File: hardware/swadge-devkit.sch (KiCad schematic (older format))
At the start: 59 parts, among them J1 USB_B_Micro, SW1 SW_SPDT, SW2 4-1437565-2, SW3 4-1437565-2, SW4 4-1437565-2, SW5 4-1437565-2, U1 ESP-12F, U2 MCP6001-OT, U3 MSA300, U4 AP1117-33, U5 BUS_PCIexpress, U6 DISP_OLED_UG-2864HSWEG01, U7 SAO, U9 MMA8452Q

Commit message: #14 Replaced ESP-12F with ESP-WROOM-02D
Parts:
- removed U1: ESP-12F, Swadge_Parts:ESP-12E_SMD, symbol Swadge_Parts:ESP-12F
- added U?: ESP-13-WROOM-02D, Swadge_Parts:ESP-13-WROOM-02, symbol Swadge_Parts:ESP-13-WROOM-02D
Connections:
- wire segments 242 -> 245
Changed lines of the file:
@@
 	1    0    0    -1
 $EndComp
-Text GLabel 1150 3150 0    50   Input ~ 0
-ADC_PIN
-Text GLabel 1150 3450 0    50   Input ~ 0
-AUD_PWR
 $Comp
 L Swadge_Parts:R_US R1
@@
 F 3 "" H 2800 1500 50  0001 C CNN
 	1    2800 1500
-	1    0    0    -1
-$EndComp
-$Comp
-L power:GND #PWR0102
-U 1 1 5C3A2494
-P 3050 3750
-F 0 "#PWR0102" H 3050 3500 50  0001 C CNN
-F 1 "GND" H 3055 3577 50  0000 C CNN
-F 2 "" H 3050 3750 50  0001 C CNN
-F 3 "" H 3050 3750 50  0001 C CNN
-	1    3050 3750
 	1    0    0    -1
 $EndComp
@@
 	1    0    0    -1
 $EndComp
-Text GLabel 3050 3150 2    50   Input ~ 0
-RX
-Text GLabel 3050 3050 2    50   Input ~ 0
-TX
 Text GLabel 3900 1300 1    50   Input ~ 0
 RX
@@
 	1    3900 1500
 	-1   0    0    1
-$EndComp
-$Comp
-L power:+3.3V #PWR0103
-U 1 1 5C3B284C
-P 600 3250
-F 0 "#PWR0103" H 600 3100 50  0001 C CNN
-F 1 "+3.3V" H 615 3423 50  0000 C CNN
-F 2 "" H 600 3250 50  0001 C CNN
-F 3 "" H 600 3250 50  0001 C CNN
-	1    600  3250
-	1    0    0    -1
 $EndComp
 Wire Notes Line
@@
 Wire Notes Line
 	3700 500  3700 2450
-Text GLabel 3050 3450 2    50   Input ~ 0
-SCL
 Wire Notes Line
 	500  7750 500  5950
@@
 Wire Notes Line
 	10000 650  10000 500
-Text GLabel 3050 3550 2    50   Input ~ 0
-SDA
 Text GLabel 7250 3250 0    50   Input ~ 0
 SW2
-Text GLabel 1150 3550 0    50   Input ~ 0
-SW4
-Text GLabel 1150 3650 0    50   Input ~ 0
-SW3
 Text GLabel 7250 5550 0    50   Input ~ 0
 SW5
@@
 	1    0    0    -1
 $EndComp
-Text GLabel 1100 3050 1    50   Input ~ 0
-REST
 Text GLabel 9000 3800 2    50   Input ~ 0
 REST
@@
 	8750 2650 8750 2500
 Wire Wire Line
-	1200 3750 600  3750
-Wire Wire Line
-	600  3750 600  3250
-Wire Wire Line
-	1200 3250 600  3250
-Connection ~ 600  3250
-Wire Wire Line
-	1200 3350 750  3350
-Wire Wire Line
-	750  3350 750  3050
-Wire Wire Line
-	750  3050 1200 3050
-Wire Wire Line
 	8950 3500 8950 3600
 Wire Wire Line
@@
 Wire Wire Line
 	2150 2200 2200 2200
-Wire Wire Line
-	1150 3150 1200 3150
-Wire Wire Line
-	1150 3450 1200 3450
-Wire Wire Line
-	1150 3550 1200 3550
-Wire Wire Line
-	1150 3650 1200 3650
-Wire Wire Line
-	3000 3050 3050 3050
-Wire Wire Line
-	3000 3150 3050 3150
-Wire Wire Line
-	3000 3250 3050 3250
-Wire Wire Line
-	3000 3350 3050 3350
-Wire Wire Line
-	3000 3450 3050 3450
-Wire Wire Line
-	3000 3550 3050 3550
-Wire Wire Line
-	3000 3650 3050 3650
-Wire Wire Line
-	3000 3750 3050 3750
 Wire Wire Line
 	1500 4950 1550 4950
@@
 Wire Notes Line
 	9850 3600 9850 3450
-$Comp
-L Swadge_Parts:ESP-12F U1
-U 1 1 5C3A0058
-P 2100 3350
-F 0 "U1" H 2100 4115 50  0000 C CNN
-F 1 "ESP-12F" H 2100 4024 50  0000 C CNN
-F 2 "Swadge_Parts:ESP-12E_SMD" H 2100 3350 50  0001 C CNN
-F 3 "https://www.elecrow.com/download/ESP-12F.pdf" H 2100 3350 50  0001 C CNN
-F 4 "260" H 0   0   50  0001 C CNN "Cost100"
-F 5 "Electrodragon SKU NWI1059" H 0   0   50  0001 C CNN "Digikey"
-F 6 "Y" H 0   0   50  0001 C CNN "Substitutable"
-	1    2100 3350
-	1    0    0    -1
-$EndComp
-Text GLabel 3050 3650 2    50   Input ~ 0
-_RES
-Text GLabel 3050 3250 2    50   Input ~ 0
-SW5
-Text GLabel 3050 3350 2    50   Input ~ 0
-SW2
 Text GLabel 1500 4950 0    50   Input ~ 0
 SCL
@@
 Wire Notes Line
 	9550 2500 10500 2500
+$Comp
+L Swadge_Parts:ESP-13-WROOM-02D U?
+U 1 1 5CD8DDB4
+P 1950 3400
+F 0 "U?" H 1925 4165 50  0000 C CNN
+F 1 "ESP-13-WROOM-02D" H 1925 4074 50  0000 C CNN
+F 2 "Swadge_Parts:ESP-13-WROOM-02" H 1850 3400 50  0001 C CNN
+F 3 "https://www.espressif.com/sites/default/files/documentation/esp-wroom-02d_esp-wroom-02u_datasheet_en.pdf" H 1850 3400 50  0001 C CNN
+F 4 "Electrodragon SKU NWI1160" H 1950 3400 50  0001 C CNN "Digikey"
+F 5 "260" H 1950 3400 50  0001 C CNN "Cost100"
+F 6 "Y" H 1950 3400 50  0001 C CNN "Substitutable"
+	1    1950 3400
+	1    0    0    -1
+$EndComp
+Text GLabel 900  3600 0    50   Input ~ 0
+_RES
+Text GLabel 900  3700 0    50   Input ~ 0
+SDA
+Text GLabel 900  3800 0    50   Input ~ 0
+SCL
+$Comp
+L power:GND #PWR?
+U 1 1 5CD8FEC8
+P 950 3950
+F 0 "#PWR?" H 950 3700 50  0001 C CNN
+F 1 "GND" H 955 3777 50  0000 C CNN
+F 2 "" H 950 3950 50  0001 C CNN
+F 3 "" H 950 3950 50  0001 C CNN
+	1    950  3950
+	1    0    0    -1
+$EndComp
+$Comp
+L power:+3.3V #PWR?
+U 1 1 5CD90854
+P 950 3050
+F 0 "#PWR?" H 950 2900 50  0001 C CNN
+F 1 "+3.3V" H 965 3223 50  0000 C CNN
+F 2 "" H 950 3050 50  0001 C CNN
+F 3 "" H 950 3050 50  0001 C CNN
+	1    950  3050
+	1    0    0    -1
+$EndComp
+Text GLabel 900  3300 0    50   Input ~ 0
+AUD_PWR
+Text GLabel 900  3400 0    50   Input ~ 0
+SW4
+Text GLabel 900  3500 0    50   Input ~ 0
+SW3
+Text GLabel 2950 3500 2    50   Input ~ 0
+SW5
+Text GLabel 2950 3900 2    50   Input ~ 0
+SW2
+Text GLabel 2950 3700 2    50   Input ~ 0
+TX
+Text GLabel 2950 3800 2    50   Input ~ 0
+RX
+Text GLabel 3350 3200 2    50   Input ~ 0
+REST
+Text GLabel 2950 3300 2    50   Input ~ 0
+ADC_PIN
+Wire Wire Line
+	2900 3200 3350 3200
+Wire Wire Line
+	3350 3200 3350 3400
+Wire Wire Line
+	3350 3400 2900 3400
+$Comp
+L power:GND #PWR?
+U 1 1 5CDDA877
+P 1950 4350
+F 0 "#PWR?" H 1950 4100 50  0001 C CNN
+F 1 "GND" H 1955 4177 50  0000 C CNN
+F 2 "" H 1950 4350 50  0001 C CNN
+F 3 "" H 1950 4350 50  0001 C CNN
+	1    1950 4350
+	1    0    0    -1
+$EndComp
+$Comp
+L power:GND #PWR?
+U 1 1 5CDDAE0D
+P 3200 3600
+F 0 "#PWR?" H 3200 3350 50  0001 C CNN
+F 1 "GND" H 3205 3427 50  0000 C CNN
+F 2 "" H 3200 3600 50  0001 C CNN
+F 3 "" H 3200 3600 50  0001 C CNN
+	1    3200 3600
+	1    0    0    -1
+$EndComp
+$Comp
+L power:GND #PWR?
+U 1 1 5CDDBB5A
+P 3050 2950
+F 0 "#PWR?" H 3050 2700 50  0001 C CNN
+F 1 "GND" H 3055 2777 50  0000 C CNN
+F 2 "" H 3050 2950 50  0001 C CNN
+F 3 "" H 3050 2950 50  0001 C CNN
+	1    3050 2950
+	1    0    0    -1
+$EndComp
+Wire Wire Line
+	950  3050 950  3100
+Wire Wire Line
+	950  3300 900  3300
+Wire Wire Line
+	900  3400 950  3400
+Wire Wire Line
+	950  3500 900  3500
+Wire Wire Line
+	900  3600 950  3600
+Wire Wire Line
+	950  3700 900  3700
+Wire Wire Line
+	900  3800 950  3800
+Wire Wire Line
+	950  3900 950  3950
+Wire Wire Line
+	1950 4300 1950 4350
+Wire Wire Line
+	2900 3900 2950 3900
+Wire Wire Line
+	2950 3800 2900 3800
+Wire Wire Line
+	2900 3700 2950 3700
+Wire Wire Line
+	2900 3600 3200 3600
+Wire Wire Line
+	2900 3500 2950 3500
+Wire Wire Line
+	2900 3300 2950 3300
+Wire Wire Line
+	2900 3100 2900 2950
+Wire Wire Line
+	2900 2950 3050 2950
+Wire Wire Line
+	950  3200 950  3100
+Connection ~ 950  3100
 $EndSCHEMATC

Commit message: one more save
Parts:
- gave numbers to parts that had none: 1
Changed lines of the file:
@@
 	4900 4150 4900 4250
 $Comp
-L power:GND #PWR?
+L power:GND #PWR0102
 U 1 1 5CCC3879
 P 4750 4850
-F 0 "#PWR?" H 4750 4600 50  0001 C CNN
+F 0 "#PWR0102" H 4750 4600 50  0001 C CNN
 F 1 "GND" H 4755 4677 50  0000 C CNN
 F 2 "" H 4750 4850 50  0001 C CNN
@@
 	9550 2500 10500 2500
 $Comp
-L Swadge_Parts:ESP-13-WROOM-02D U?
+L Swadge_Parts:ESP-13-WROOM-02D U1
 U 1 1 5CD8DDB4
 P 1950 3400
-F 0 "U?" H 1925 4165 50  0000 C CNN
+F 0 "U1" H 1925 4165 50  0000 C CNN
 F 1 "ESP-13-WROOM-02D" H 1925 4074 50  0000 C CNN
 F 2 "Swadge_Parts:ESP-13-WROOM-02" H 1850 3400 50  0001 C CNN
@@
 SCL
 $Comp
-L power:GND #PWR?
+L power:GND #PWR0103
 U 1 1 5CD8FEC8
 P 950 3950
-F 0 "#PWR?" H 950 3700 50  0001 C CNN
+F 0 "#PWR0103" H 950 3700 50  0001 C CNN
 F 1 "GND" H 955 3777 50  0000 C CNN
 F 2 "" H 950 3950 50  0001 C CNN
@@
 $EndComp
 $Comp
-L power:+3.3V #PWR?
+L power:+3.3V #PWR0118
 U 1 1 5CD90854
 P 950 3050
-F 0 "#PWR?" H 950 2900 50  0001 C CNN
+F 0 "#PWR0118" H 950 2900 50  0001 C CNN
 F 1 "+3.3V" H 965 3223 50  0000 C CNN
 F 2 "" H 950 3050 50  0001 C CNN
@@
 	3350 3400 2900 3400
 $Comp
-L power:GND #PWR?
+L power:GND #PWR0119
 U 1 1 5CDDA877
 P 1950 4350
-F 0 "#PWR?" H 1950 4100 50  0001 C CNN
+F 0 "#PWR0119" H 1950 4100 50  0001 C CNN
 F 1 "GND" H 1955 4177 50  0000 C CNN
 F 2 "" H 1950 4350 50  0001 C CNN
@@
 $EndComp
 $Comp
-L power:GND #PWR?
+L power:GND #PWR0120
 U 1 1 5CDDAE0D
 P 3200 3600
-F 0 "#PWR?" H 3200 3350 50  0001 C CNN
+F 0 "#PWR0120" H 3200 3350 50  0001 C CNN
 F 1 "GND" H 3205 3427 50  0000 C CNN
 F 2 "" H 3200 3600 50  0001 C CNN
@@
 $EndComp
 $Comp
-L power:GND #PWR?
+L power:GND #PWR0121
 U 1 1 5CDDBB5A
 P 3050 2950
-F 0 "#PWR?" H 3050 2700 50  0001 C CNN
+F 0 "#PWR0121" H 3050 2700 50  0001 C CNN
 F 1 "GND" H 3055 2777 50  0000 C CNN
 F 2 "" H 3050 2950 50  0001 C CNN

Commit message: #9 #11 #13 #14 #15 Routed everything
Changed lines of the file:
@@
 EESchema Schematic File Version 4
+LIBS:swadge-devkit-cache
 EELAYER 29 0
 EELAYER END
@@
 Text GLabel 900  3300 0    50   Input ~ 0
 AUD_PWR
+Text GLabel 2950 3900 2    50   Input ~ 0
+SW4
 Text GLabel 900  3400 0    50   Input ~ 0
-SW4
-Text GLabel 900  3500 0    50   Input ~ 0
 SW3
 Text GLabel 2950 3500 2    50   Input ~ 0
 SW5
-Text GLabel 2950 3900 2    50   Input ~ 0
+Text GLabel 900  3500 0    50   Input ~ 0
 SW2
 Text GLabel 2950 3700 2    50   Input ~ 0

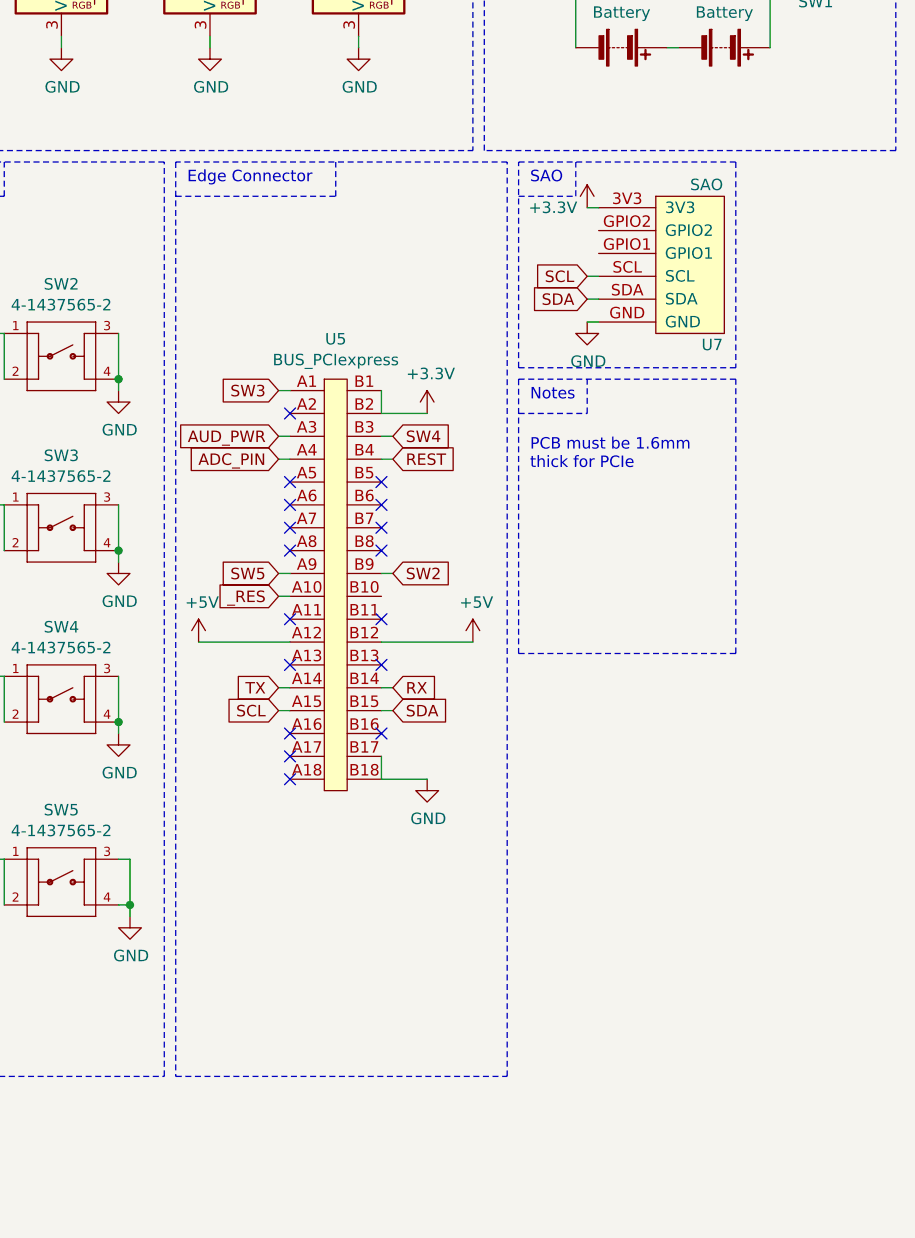
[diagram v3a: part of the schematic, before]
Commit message: #17 Reordered PCIe connector for WROOM sanity
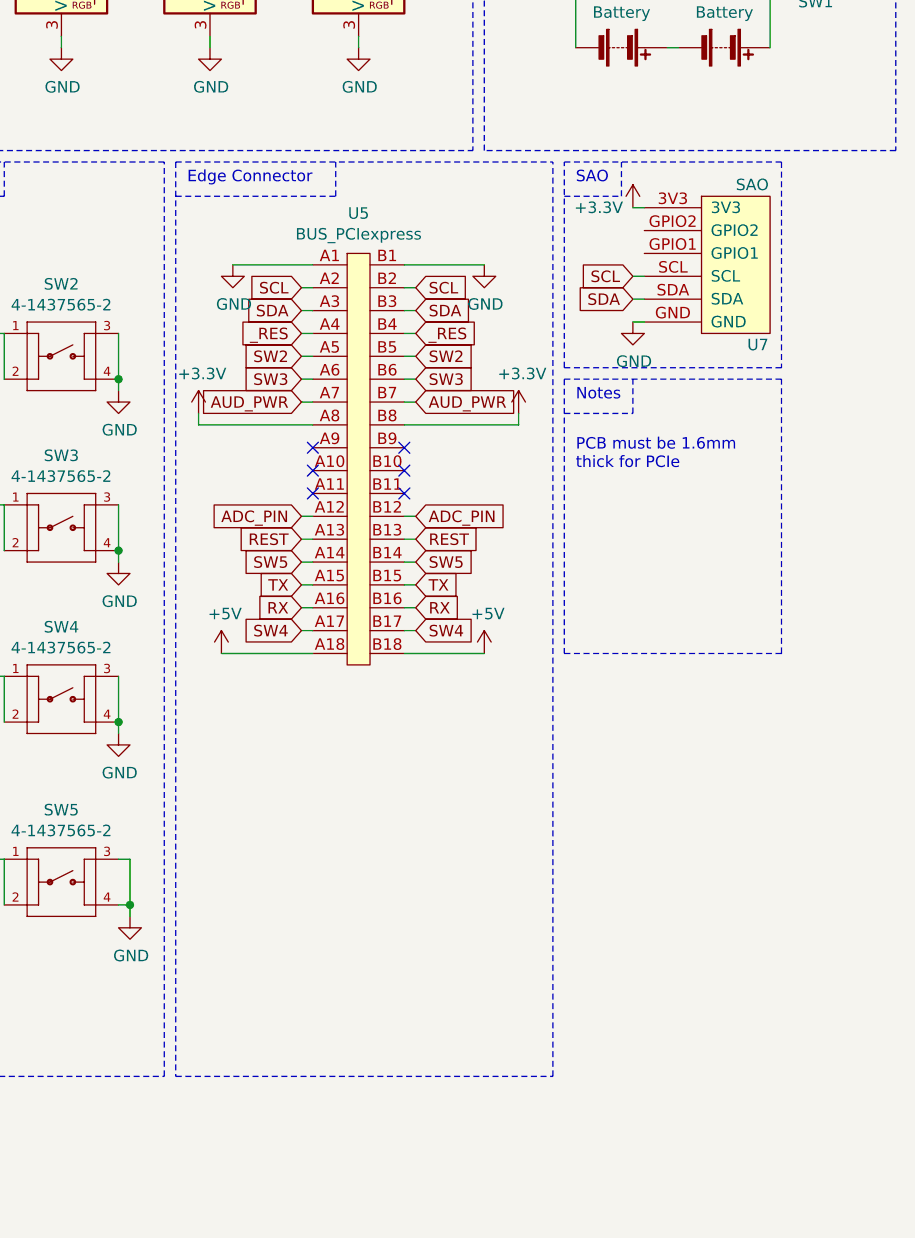
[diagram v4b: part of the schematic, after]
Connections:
- wire segments 245 -> 259
- no-connect marks 27 -> 16
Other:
- moved on the sheet: U5, U7

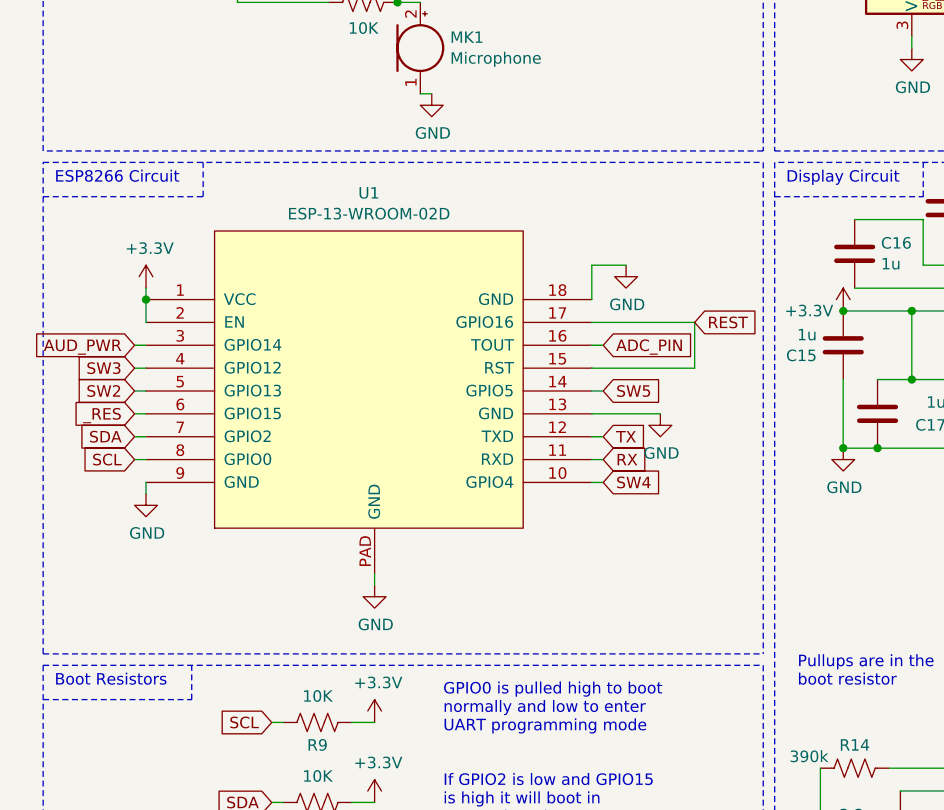
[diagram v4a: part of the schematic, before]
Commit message: #18 Add caps to WROOM power lines
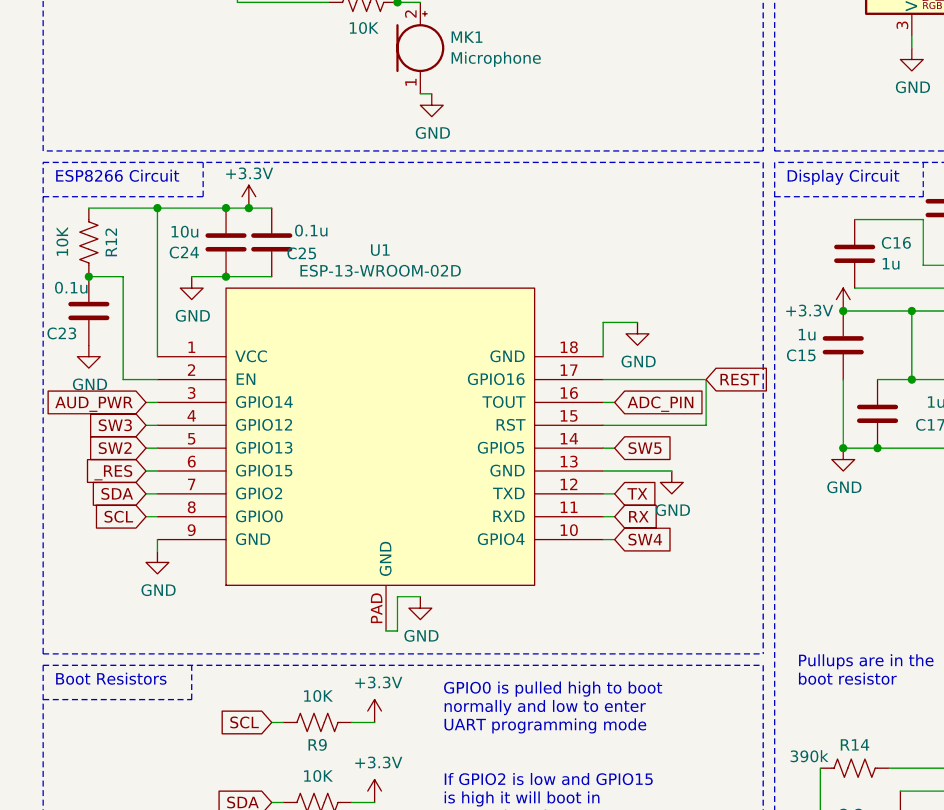
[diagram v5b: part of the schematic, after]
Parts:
- added C23, C25: 0.1u, Swadge_Parts:C_0603_1608Metric, symbol Swadge_Parts:C
- added C24: 10u, Swadge_Parts:C_0603_1608Metric, symbol Swadge_Parts:C
- added R12: 10K, Swadge_Parts:R_0603_1608Metric, symbol Swadge_Parts:R_US
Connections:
- wire segments 259 -> 269
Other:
- moved on the sheet: U1

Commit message: #19 Update AA holder footprints, move them further apart too
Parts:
- BT1, BT2: footprint Swadge_Parts:BCAAPC -> Swadge_Parts:2460; Cost100 114 -> 116; Digikey BCAAPC-ND -> 36-2460-ND
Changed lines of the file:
@@
 EESchema Schematic File Version 4
+LIBS:swadge-devkit-cache
 EELAYER 29 0
 EELAYER END
@@
 F 0 "BT2" V 10205 2000 50  0000 C CNN
 F 1 "Battery" V 10296 2000 50  0000 C CNN
-F 2 "Swadge_Parts:BCAAPC" V 10450 2060 50  0001 C CNN
-F 3 "http://www.memoryprotectiondevices.com/datasheets/BCAAPC-datasheet.pdf" V 10450 2060 50  0001 C CNN
-F 4 "114" H 0   0   50  0001 C CNN "Cost100"
-F 5 "BCAAPC-ND" H 0   0   50  0001 C CNN "Digikey"
+F 2 "Swadge_Parts:2460" V 10450 2060 50  0001 C CNN
+F 3 "http://www.keyelco.com/product-pdf.cfm?p=1025" V 10450 2060 50  0001 C CNN
+F 4 "116" H 0   0   50  0001 C CNN "Cost100"
+F 5 "36-2460-ND" H 0   0   50  0001 C CNN "Digikey"
 F 6 "Y" H 0   0   50  0001 C CNN "Substitutable"
 	1    10450 2000
@@
 F 0 "BT1" V 9755 2000 50  0000 C CNN
 F 1 "Battery" V 9846 2000 50  0000 C CNN
-F 2 "Swadge_Parts:BCAAPC" V 10000 2060 50  0001 C CNN
-F 3 "http://www.memoryprotectiondevices.com/datasheets/BCAAPC-datasheet.pdf" V 10000 2060 50  0001 C CNN
-F 4 "114" H 0   0   50  0001 C CNN "Cost100"
-F 5 "BCAAPC-ND" H 0   0   50  0001 C CNN "Digikey"
+F 2 "Swadge_Parts:2460" V 10000 2060 50  0001 C CNN
+F 3 "http://www.keyelco.com/product-pdf.cfm?p=1025" V 10000 2060 50  0001 C CNN
+F 4 "116" H 0   0   50  0001 C CNN "Cost100"
+F 5 "36-2460-ND" H 0   0   50  0001 C CNN "Digikey"
 F 6 "Y" H 0   0   50  0001 C CNN "Substitutable"
 	1    10000 2000

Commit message: Updated WROOM with digikey p/n. Tweaked layout
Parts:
- U1: Cost100 260 -> 270; Digikey Electrodragon SKU NWI1160 -> 1904-1021-1-ND
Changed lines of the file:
@@
 F 2 "Swadge_Parts:ESP-13-WROOM-02" H 1900 3650 50  0001 C CNN
 F 3 "https://www.espressif.com/sites/default/files/documentation/esp-wroom-02d_esp-wroom-02u_datasheet_en.pdf" H 1900 3650 50  0001 C CNN
-F 4 "Electrodragon SKU NWI1160" H 2000 3650 50  0001 C CNN "Digikey"
-F 5 "260" H 2000 3650 50  0001 C CNN "Cost100"
+F 4 "1904-1021-1-ND" H 2000 3650 50  0001 C CNN "Digikey"
+F 5 "270" H 2000 3650 50  0001 C CNN "Cost100"
 F 6 "Y" H 2000 3650 50  0001 C CNN "Substitutable"
 	1    2000 3650

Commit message: Added Gainsil GS321-TR opamp
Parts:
- removed U2: MCP6001-OT, Swadge_Parts:SOT-23-5, symbol Swadge_Parts:MCP6001UT-I_OT
- added U1: GS321-TR, Swadge_Parts:SOT-23-5, symbol Swadge_Parts:GS321-TR
- renumbered C2 to C1, C1 to C10, C3 to C11, C19 to C12, C24 to C13, C25 to C14, C16 to C15, C23 to C16, C15 to C17, C17 to C18, C18 to C19, C4 to C2, C14 to C21, C21 to C22, C13 to C23, C22 to C24, C12 to C25, C5 to C3, C6 to C4, C7 to C5, C8 to C6, C9 to C7, C10 to C8, C11 to C9, R9 to R10, R14 to R11, R10 to R12, R11 to R13, R4 to R3, R6 to R4, R3 to R5, R7 to R6, R8 to R7, R5 to R8, R12 to R9, U4 to U2, U7 to U3, U1 to U4, U9 to U7, U3 to U8
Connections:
- wire segments 269 -> 274
- no-connect marks 16 -> 18
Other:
- moved on the sheet: R1
